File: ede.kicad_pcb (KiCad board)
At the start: 4 copper layers, 72.1 x 49 mm, 114 parts, among them J1 Conn_01x01, J10 Conn_01x01, J11 Conn_01x01, J12 Conn_01x01, J2 Conn_01x01, J3 Conn_01x01, J4 Conn_01x01, J5 Conn_01x06, J6 Conn_01x01, J7 Conn_01x04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

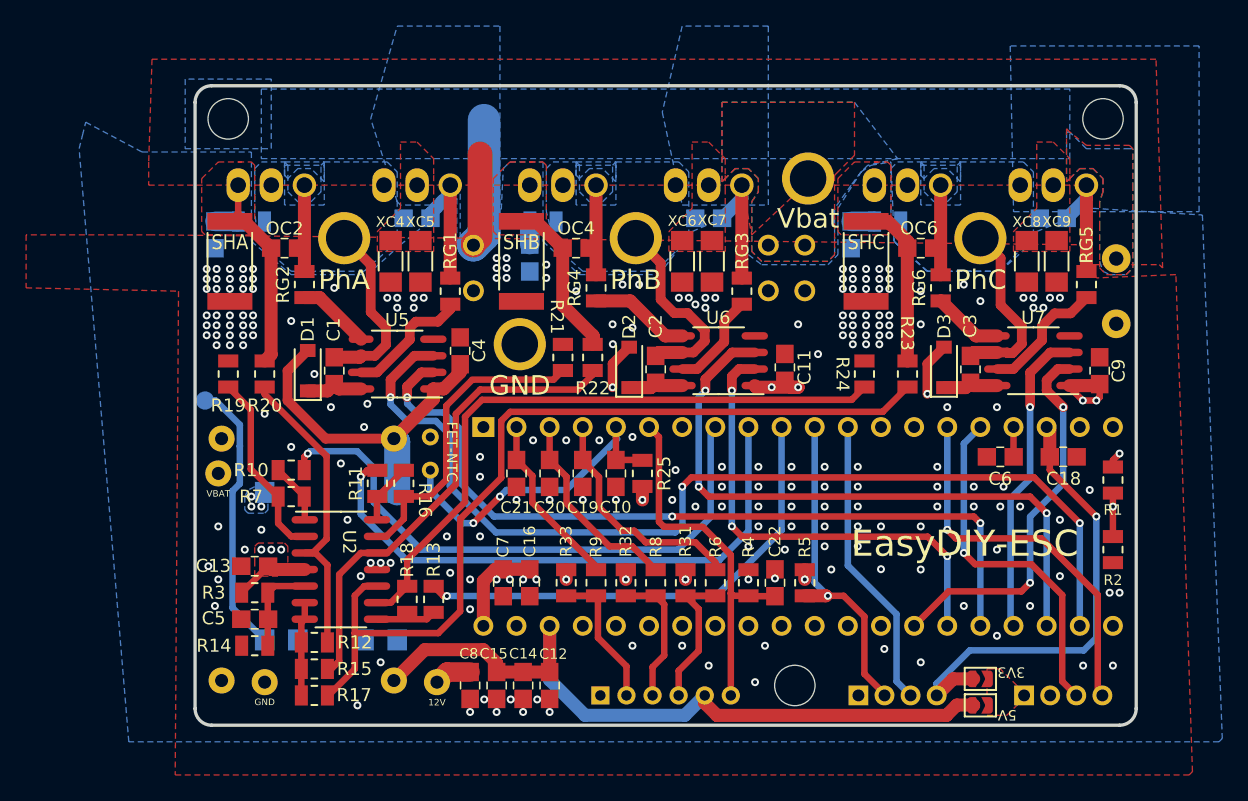
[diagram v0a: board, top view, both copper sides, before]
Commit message: pcb: alter some of the R0805 footprint as per reference
Signed-off-by: Afzal <afzal@intible.in>
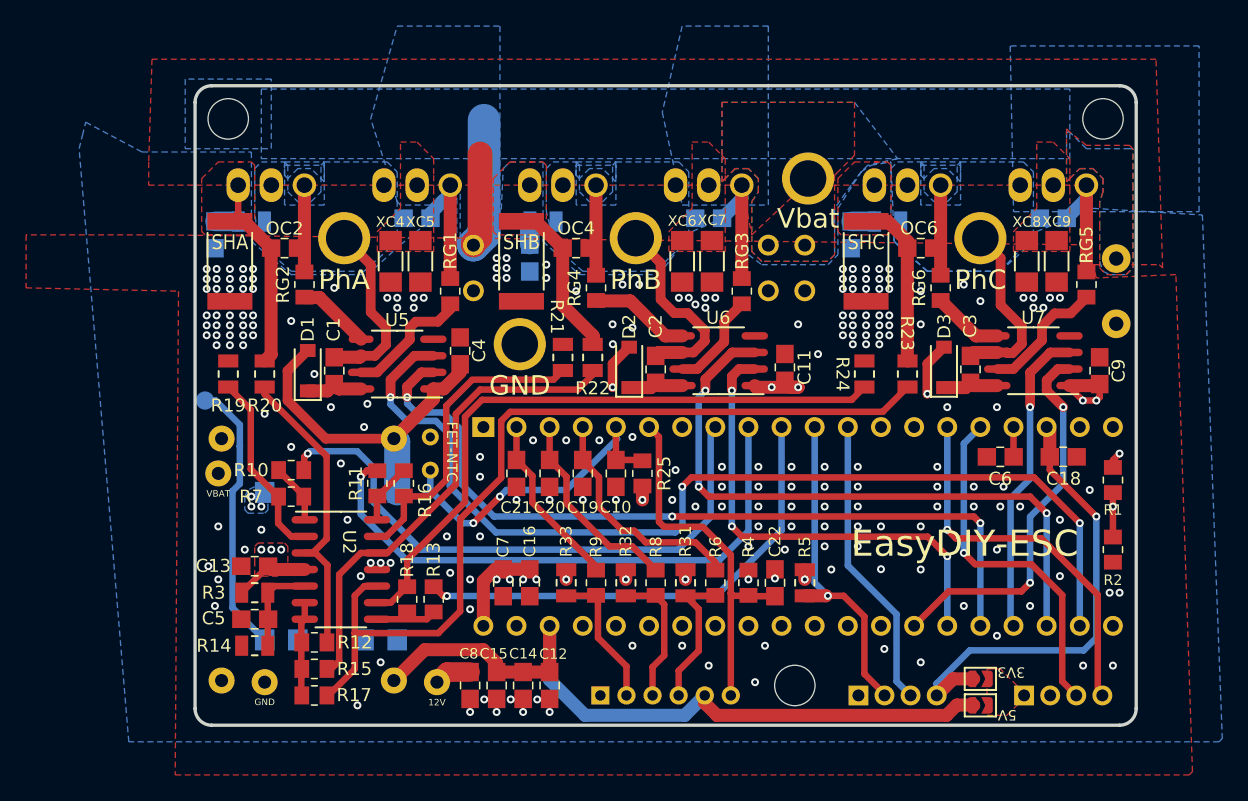
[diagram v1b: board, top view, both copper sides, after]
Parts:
- R1, R10, R11, R12, R13, R15, R16, R17, R18, R2, R25, R4, R6, R7, R8, R9, RG1, RG2, RG3, RG4, RG5, RG6: footprint Intible:R_0805_2012Metric_EDE -> Intible:R_0805_2012Metric_small_EDE
